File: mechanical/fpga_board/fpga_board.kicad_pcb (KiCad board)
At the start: 4 copper layers, 100 x 100 mm, 36 parts, among them J1 Conn_02x17_Odd_Even, J2 Conn_02x17_Odd_Even, J3 Conn_02x17_Odd_Even, J4 Conn_02x17_Odd_Even, J5 Conn_02x17_Odd_Even, J6 jtag, J7 Conn_02x03_Odd_Even, U1 XC6SLX16-FTG256

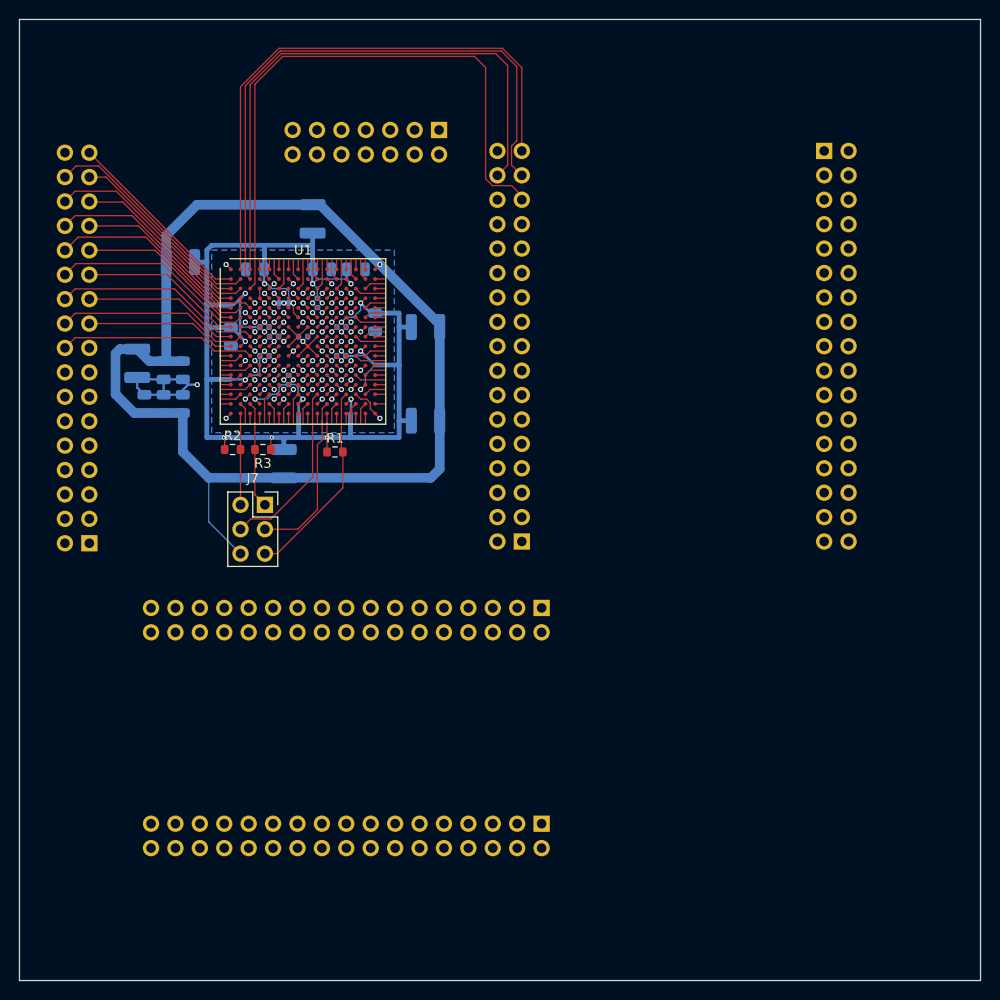
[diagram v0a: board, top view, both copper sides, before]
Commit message: all fpga pins routed, still need regulators
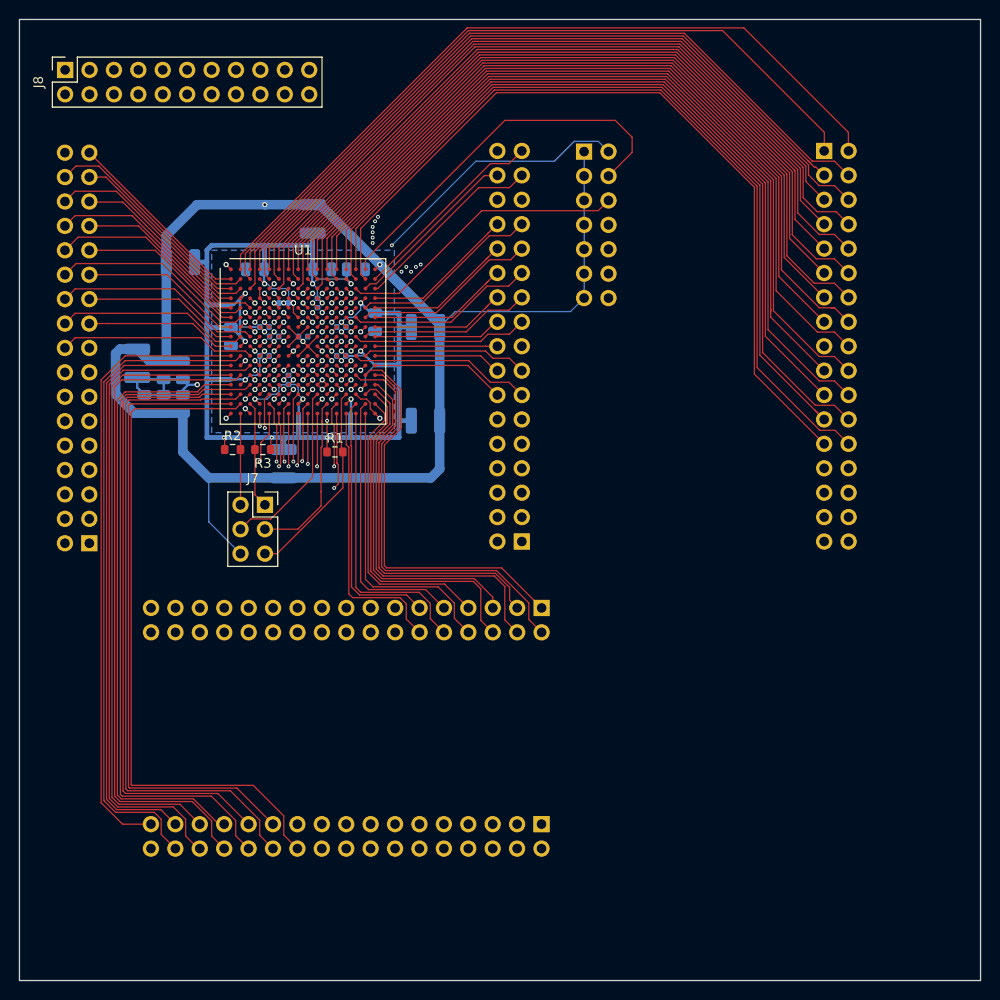
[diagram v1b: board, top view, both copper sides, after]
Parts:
- added J8: Conn_02x12_Odd_Even, Connector_PinSocket_2.54mm:PinSocket_2x11_P2.54mm_Vertical, F.Cu at (243.3, 160.0)
- moved J6 15.3 mm to (297.3, 168.5), turned to 180 degrees
- moved J4 0.05 mm to (292.9, 238.5)
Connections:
- U1 pad A10: Net-(U1-PadA10) -> /T16+3
- U1 pad A11: Net-(U1-PadA11) -> /T12+3
- U1 pad A12: Net-(U1-PadA12) -> /T11+3
- U1 pad A13: Net-(U1-PadA13) -> /T13+3
- U1 pad A14: Net-(U1-PadA14) -> /T16-3
- U1 pad A2: /T9-1 -> /T5+3
- U1 pad A3: /T13-1 -> /T6+3
- U1 pad A4: /T14-1 -> /T7+3
- U1 pad A5: Net-(U1-PadA5) -> /T8+3
- U1 pad A6: Net-(U1-PadA6) -> /T5-3
- U1 pad A7: Net-(U1-PadA7) -> /T6-3
- U1 pad A8: Net-(U1-PadA8) -> /T7-3
- U1 pad A9: Net-(U1-PadA9) -> /T8-3
- U1 pad B10: Net-(U1-PadB10) -> /T4-3
- U1 pad B12: Net-(U1-PadB12) -> /T14+3
- U1 pad B14: Net-(U1-PadB14) -> /T10+3
- U1 pad B15: Net-(U1-PadB15) -> /T9+3
- U1 pad B16: Net-(U1-PadB16) -> /T9-1
- U1 pad B3: /T10-1 -> /T1+3
- U1 pad B5: Net-(U1-PadB5) -> /T3+3
- U1 pad B6: Net-(U1-PadB6) -> /T4+3
- U1 pad B8: Net-(U1-PadB8) -> /T2-3
- U1 pad C10: Net-(U1-PadC10) -> /T15+3
- U1 pad C11: Net-(U1-PadC11) -> /T11-3
- U1 pad C13: Net-(U1-PadC13) -> /extra19
- U1 pad C15: Net-(U1-PadC15) -> /T13-1
- U1 pad C16: Net-(U1-PadC16) -> /T10-1
- U1 pad C3: /T11-1 -> /T2+3
- U1 pad C5: Net-(U1-PadC5) -> /extra5
- U1 pad C6: Net-(U1-PadC6) -> /T1-3
- U1 pad C7: Net-(U1-PadC7) -> /extra9
- U1 pad C8: Net-(U1-PadC8) -> /T3-3
- U1 pad C9: Net-(U1-PadC9) -> /T15-3
- U1 pad D11: Net-(U1-PadD11) -> /T10-3
- U1 pad D12: Net-(U1-PadD12) -> /T9-3
- U1 pad D14: Net-(U1-PadD14) -> /T14-1
- U1 pad D16: Net-(U1-PadD16) -> /T15-1
- U1 pad D5: Net-(U1-PadD5) -> /extra1
- U1 pad D6: Net-(U1-PadD6) -> /extra7
- U1 pad D8: Net-(U1-PadD8) -> /extra11
- U1 pad D9: Net-(U1-PadD9) -> /T12-3
- U1 pad E10: Net-(U1-PadE10) -> /T14-3
- U1 pad E11: Net-(U1-PadE11) -> /T13-3
- U1 pad E12: Net-(U1-PadE12) -> /T11-1
- U1 pad E13: Net-(U1-PadE13) -> /T2-1
- U1 pad E15: Net-(U1-PadE15) -> /T12-1
- U1 pad E16: Net-(U1-PadE16) -> /T16-1
- U1 pad E6: Net-(U1-PadE6) -> /extra3
- U1 pad E7: Net-(U1-PadE7) -> /extra4
- U1 pad E8: Net-(U1-PadE8) -> /extra8
- U1 pad F10: Net-(U1-PadF10) -> /extra10
- U1 pad F12: Net-(U1-PadF12) -> /extra14
- U1 pad F13: Net-(U1-PadF13) -> /T6-1
- U1 pad F14: Net-(U1-PadF14) -> /T10+1
- U1 pad F15: Net-(U1-PadF15) -> /T9+1
- U1 pad F16: Net-(U1-PadF16) -> /T13+1
- U1 pad F7: Net-(U1-PadF7) -> /extra2
- U1 pad F9: Net-(U1-PadF9) -> /extra12
- U1 pad G11: Net-(U1-PadG11) -> /extra6
- U1 pad G12: Net-(U1-PadG12) -> /extra16
- U1 pad G14: Net-(U1-PadG14) -> /T1-1
- U1 pad G16: Net-(U1-PadG16) -> /T14+1
- U1 pad H11: Net-(U1-PadH11) -> /extra13
- U1 pad H13: Net-(U1-PadH13) -> /extra15
- U1 pad H14: Net-(U1-PadH14) -> /T12+1
- U1 pad H15: Net-(U1-PadH15) -> /T11+1
- U1 pad H16: Net-(U1-PadH16) -> /T15+1
- U1 pad J11: Net-(U1-PadJ11) -> /extra17
- U1 pad J12: Net-(U1-PadJ12) -> /T5-1
- U1 pad J13: Net-(U1-PadJ13) -> /T4+1
- U1 pad J14: Net-(U1-PadJ14) -> /T8+1
- U1 pad J16: Net-(U1-PadJ16) -> /T16+1
- U1 pad K1: Net-(U1-PadK1) -> /T9-4
- U1 pad K11: Net-(U1-PadK11) -> /extra18
- U1 pad K12: Net-(U1-PadK12) -> /T3+1
- U1 pad K14: Net-(U1-PadK14) -> /T3-1
- U1 pad K15: Net-(U1-PadK15) -> /T4-1
- U1 pad K16: Net-(U1-PadK16) -> /T8-1
- U1 pad K2: Net-(U1-PadK2) -> /T13-4
- U1 pad K5: Net-(U1-PadK5) -> /T11+4
- U1 pad L1: Net-(U1-PadL1) -> /T10-4
- U1 pad L10: Net-(U1-PadL10) -> /T2+4
- U1 pad L12: Net-(U1-PadL12) -> /T6+1
- U1 pad L13: Net-(U1-PadL13) -> /T7+1
- U1 pad L14: Net-(U1-PadL14) -> /T2+1
- U1 pad L16: Net-(U1-PadL16) -> /T7-1
- U1 pad L3: Net-(U1-PadL3) -> /T14-4
- U1 pad L5: Net-(U1-PadL5) -> /T12+4
- U1 pad L7: Net-(U1-PadL7) -> /T4+4
- U1 pad L8: Net-(U1-PadL8) -> /T3+4
- U1 pad M1: Net-(U1-PadM1) -> /T11-4
- U1 pad M10: Net-(U1-PadM10) -> /T6+4
- U1 pad M11: Net-(U1-PadM11) -> /T1+4
- U1 pad M12: Net-(U1-PadM12) -> /T5+4
- U1 pad M13: Net-(U1-PadM13) -> /T1+1
- U1 pad M14: Net-(U1-PadM14) -> /T2+5
- U1 pad M15: Net-(U1-PadM15) -> /T1+5
- U1 pad M16: Net-(U1-PadM16) -> /T5+5
- U1 pad M2: Net-(U1-PadM2) -> /T15-4
- U1 pad M3: Net-(U1-PadM3) -> /T16+4
- U1 pad M4: Net-(U1-PadM4) -> /T15+4
- U1 pad M5: Net-(U1-PadM5) -> /T4-4
- U1 pad M6: Net-(U1-PadM6) -> /T6-4
- U1 pad M7: Net-(U1-PadM7) -> /T7+4
- U1 pad M9: Net-(U1-PadM9) -> /T15+5
- U1 pad N1: Net-(U1-PadN1) -> /T12-4
- U1 pad N12: Net-(U1-PadN12) -> /T3-5
- U1 pad N14: Net-(U1-PadN14) -> /T5+1
- U1 pad N16: Net-(U1-PadN16) -> /T6+5
- U1 pad N3: Net-(U1-PadN3) -> /T16-4
- U1 pad N4: Net-(U1-PadN4) -> /T8-4
- U1 pad N5: Net-(U1-PadN5) -> /T5-4
- U1 pad N6: Net-(U1-PadN6) -> /T14+5
- U1 pad N8: Net-(U1-PadN8) -> /T12+5
- U1 pad N9: Net-(U1-PadN9) -> /T8-5
- U1 pad P1: Net-(U1-PadP1) -> /T9+4
- U1 pad P11: Net-(U1-PadP11) -> /T7-5
- U1 pad P12: Net-(U1-PadP12) -> /T4-5
- U1 pad P15: Net-(U1-PadP15) -> /T3+5
- U1 pad P16: Net-(U1-PadP16) -> /T7+5
- U1 pad P2: Net-(U1-PadP2) -> /T13+4
- U1 pad P4: Net-(U1-PadP4) -> /T7-4
- U1 pad P5: Net-(U1-PadP5) -> /T8+4
- U1 pad P6: Net-(U1-PadP6) -> /T2-4
- U1 pad P7: Net-(U1-PadP7) -> /T11+5
- U1 pad P8: Net-(U1-PadP8) -> /T15-5
- U1 pad P9: Net-(U1-PadP9) -> /T16+5
- U1 pad R1: Net-(U1-PadR1) -> /T10+4
- U1 pad R12: Net-(U1-PadR12) -> /T10+5
- U1 pad R14: Net-(U1-PadR14) -> /T2-5
- U1 pad R15: Net-(U1-PadR15) -> /T1-5
- U1 pad R16: Net-(U1-PadR16) -> /T4+5
- U1 pad R2: Net-(U1-PadR2) -> /T14+4
- U1 pad R5: Net-(U1-PadR5) -> /T13-5
- U1 pad R7: Net-(U1-PadR7) -> /T14-5
- U1 pad R9: Net-(U1-PadR9) -> /T16-5
- U1 pad T10: Net-(U1-PadT10) -> /T13+5
- U1 pad T12: Net-(U1-PadT12) -> /extra20
- U1 pad T13: Net-(U1-PadT13) -> /T6-5
- U1 pad T14: Net-(U1-PadT14) -> /T5-5
- U1 pad T15: Net-(U1-PadT15) -> /T8+5
- U1 pad T3: Net-(U1-PadT3) -> /T3-4
- U1 pad T4: Net-(U1-PadT4) -> /T1-4
- U1 pad T5: Net-(U1-PadT5) -> /T9-5
- U1 pad T6: Net-(U1-PadT6) -> /T10-5
- U1 pad T7: Net-(U1-PadT7) -> /T11-5
- U1 pad T8: Net-(U1-PadT8) -> /T12-5
- U1 pad T9: Net-(U1-PadT9) -> /T9+5
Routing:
- net /T5+4: track 0.00 -> 110.5 mm, vias 0 -> 1
- net /T1+4: track 0.00 -> 109.6 mm, vias 0 -> 1
- net /T13-3: track 0.00 -> 109.6 mm, vias 0 -> 1
- net /T9-3: track 0.00 -> 108.2 mm, vias 0 -> 1
- net /T14-3: track 0.00 -> 107.6 mm, vias 0 -> 1
- net /T15-3: track 0.00 -> 105.9 mm, vias 0 -> 1
- net /T6+4: track 0.00 -> 105.6 mm, vias 0 -> 1
- net /T2+4: track 0.00 -> 105.2 mm, vias 0 -> 1
- net /T10-3: track 0.00 -> 104.2 mm, vias 0 -> 1
- net /T11-3: track 0.00 -> 103.5 mm, vias 0 -> 1
- net /T12-3: track 0.00 -> 103.2 mm, vias 0 -> 1
- net /T7+4: track 0.00 -> 101.5 mm, vias 0 -> 1
- net /T3+4: track 0.00 -> 100.5 mm, vias 0 -> 1
- net /T4+4: track 0.00 -> 96.5 mm, vias 0 -> 1
- net /T8+4: track 0.00 -> 91.6 mm, vias 0 -> 1
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
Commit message: Moved FPGA and added hole
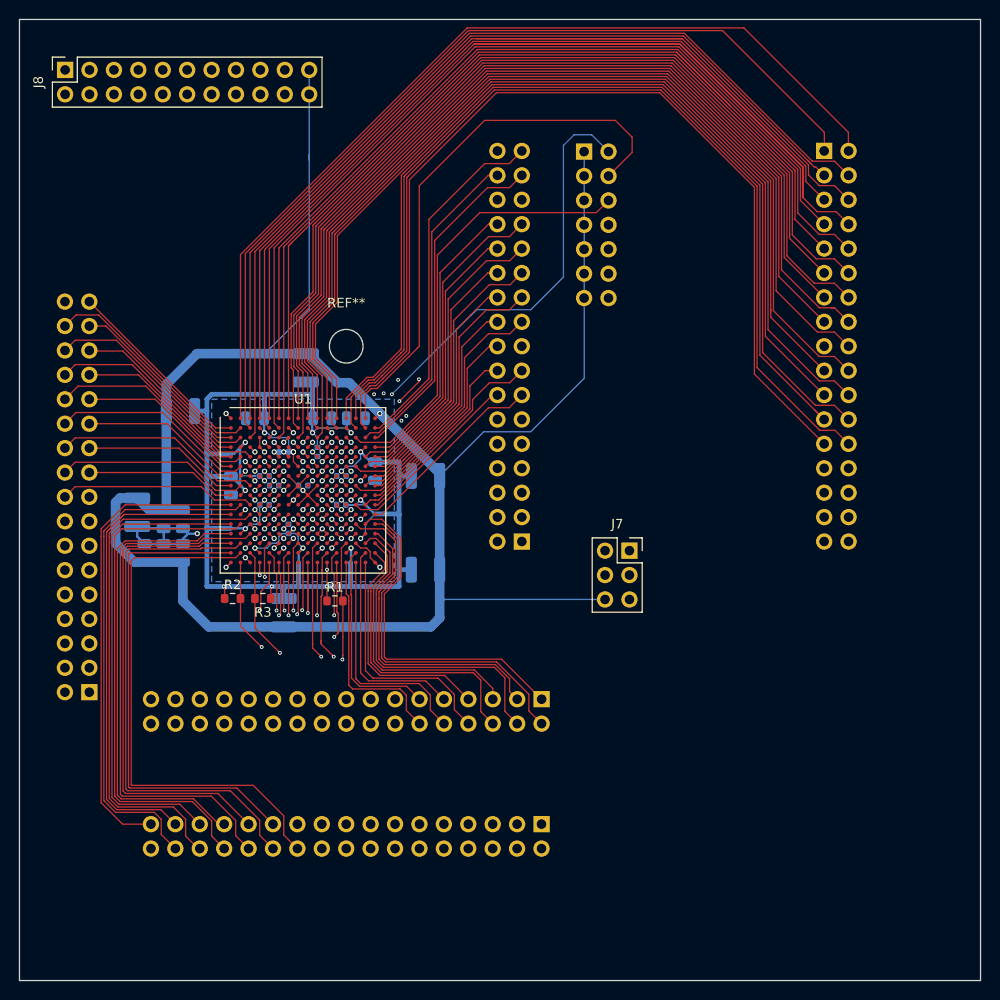
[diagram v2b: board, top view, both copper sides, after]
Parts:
- added REF**: MountingHole_3.5mm, MountingHole:MountingHole_3.5mm, F.Cu at (272.5, 188.7)
- moved J7 38.2 mm to (302.0, 210.0)
- moved C11 15.5 mm to (268.3, 191.0)
- moved C1 15.5 mm to (280.8, 212.0)
- moved C10 15.5 mm to (266.5, 207.7)
- moved C12 15.5 mm to (270.0, 196.2)
- moved C13 15.5 mm to (264.0, 205.2)
- moved C14 15.5 mm to (264.0, 202.2)
- moved C15 15.5 mm to (280.8, 202.2)
- moved C16 15.5 mm to (260.5, 203.2)
- moved C17 15.5 mm to (266.0, 199.7)
- moved C18 15.5 mm to (265.0, 203.2)
- moved C19 15.5 mm to (268.1, 203.2)
- moved C2 15.5 mm to (273.5, 196.2)
- moved C20 15.5 mm to (255.5, 206.7)
- moved C21 15.5 mm to (253.5, 210.2)
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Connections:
- U1 pad E13: /T2-1 -> /T6-1
- U1 pad F13: /T6-1 -> /T2-1
- U1 pad G14: /T1-1 -> /T5-1
- U1 pad J11: /extra17 -> /glckorsomething
- U1 pad J12: /T5-1 -> /T1-1
- U1 pad J13: /T4+1 -> /T8+1
- U1 pad J14: /T8+1 -> /T4+1
- U1 pad K12: /T3+1 -> /T7+1
- U1 pad K14: /T3-1 -> /T7-1
- U1 pad K15: /T4-1 -> /T8-1
- U1 pad K16: /T8-1 -> /T4-1
- U1 pad L12: /T6+1 -> /T2+1
- U1 pad L13: /T7+1 -> /T3+1
- U1 pad L14: /T2+1 -> /T6+1
- U1 pad L16: /T7-1 -> /T3-1
- U1 pad M13: /T1+1 -> /T5+1
- U1 pad N14: /T5+1 -> /T1+1
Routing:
- net /T8+3: track 80.8 -> 139.1 mm
- net /init_b: track 11.1 -> 53.1 mm, vias 0 -> 1
- net /program_b: track 9.50 -> 49.6 mm, vias 0 -> 1
- net /T7+3: track 79.9 -> 119.0 mm
- net /gnd: track 195.2 -> 231.3 mm, vias 26 -> 25
- net /cclk: track 18.0 -> 47.7 mm, vias 0 -> 1
- net /din: track 18.6 -> 47.3 mm, vias 0 -> 1
- net /extra6: track 37.7 -> 61.8 mm
- net /done: track 21.0 -> 45.0 mm, vias 0 -> 1
- net /T1-3: track 80.7 -> 104.2 mm
- net /extra19: track 42.3 -> 63.7 mm
- net /extra10: track 30.9 -> 50.0 mm
- net /extra20: track 71.7 -> 89.7 mm, vias 3 -> 1
- net /extra12: track 31.6 -> 49.6 mm
- net /extra8: track 31.8 -> 49.7 mm
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
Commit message: Added mounting holes, reduced size on FPGA board
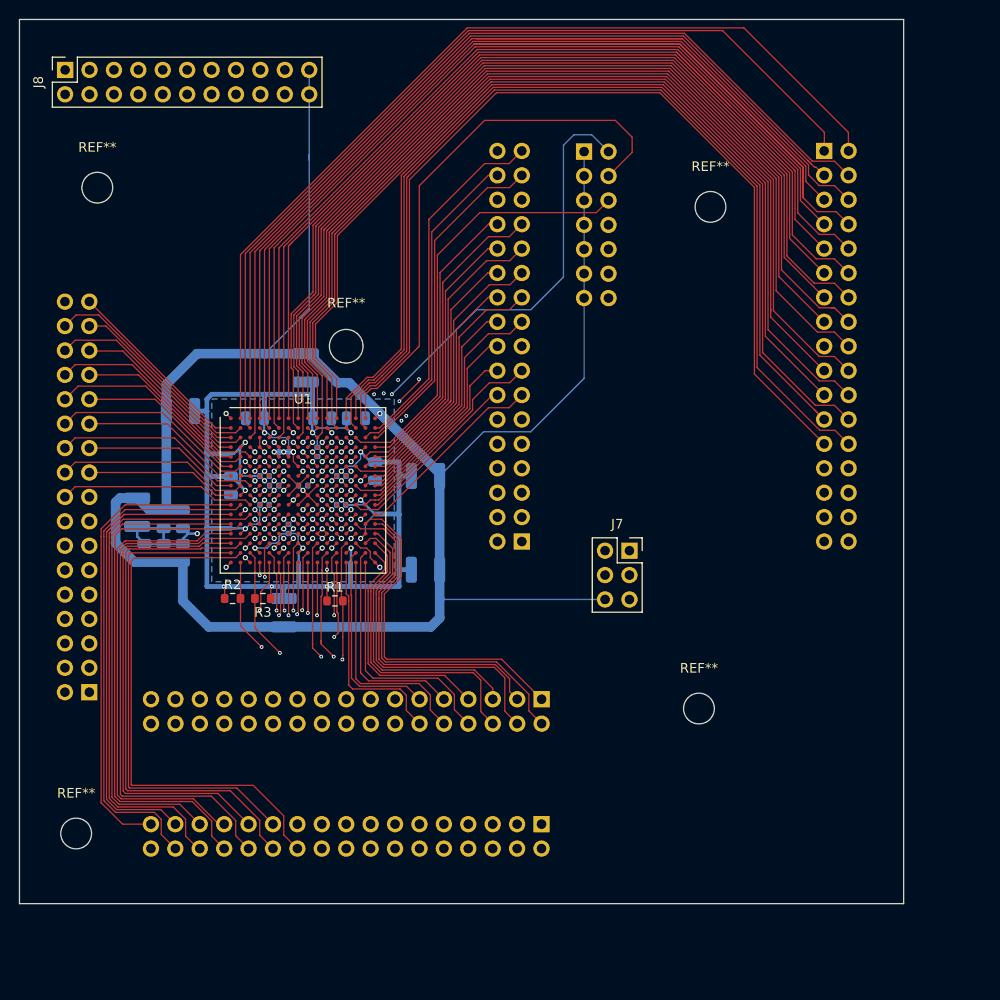
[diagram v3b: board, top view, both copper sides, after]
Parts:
- added REF**: MountingHole_3.2mm_M3, MountingHole:MountingHole_3.2mm_M3, F.Cu at (244.4, 239.4)
- added REF**: MountingHole_3.2mm_M3, MountingHole:MountingHole_3.2mm_M3, F.Cu at (309.2, 226.4)
- added REF**: MountingHole_3.2mm_M3, MountingHole:MountingHole_3.2mm_M3, F.Cu at (310.4, 174.2)
- added REF**: MountingHole_3.2mm_M3, MountingHole:MountingHole_3.2mm_M3, F.Cu at (246.6, 172.2)
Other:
- board size 100 x 100 mm -> 92 x 92 mm

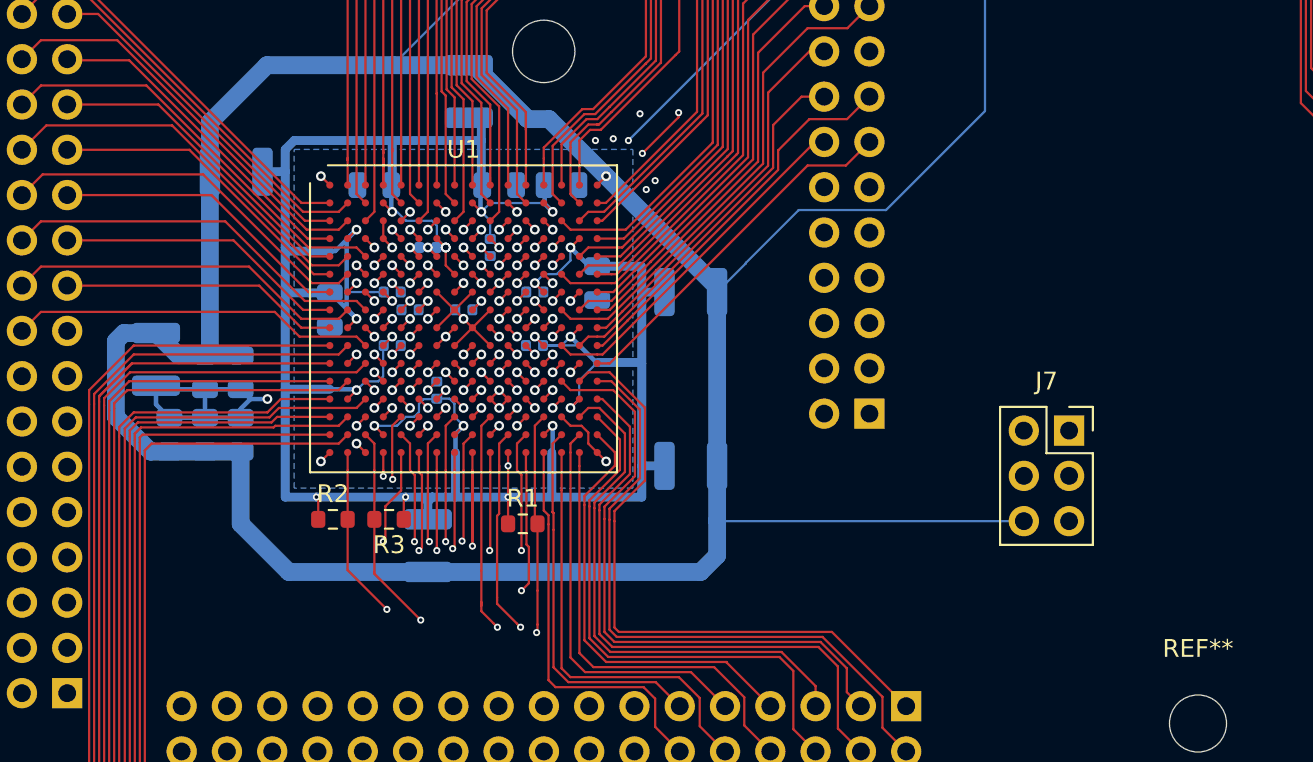
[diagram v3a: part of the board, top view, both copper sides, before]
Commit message: Added linear regulators and oscillator
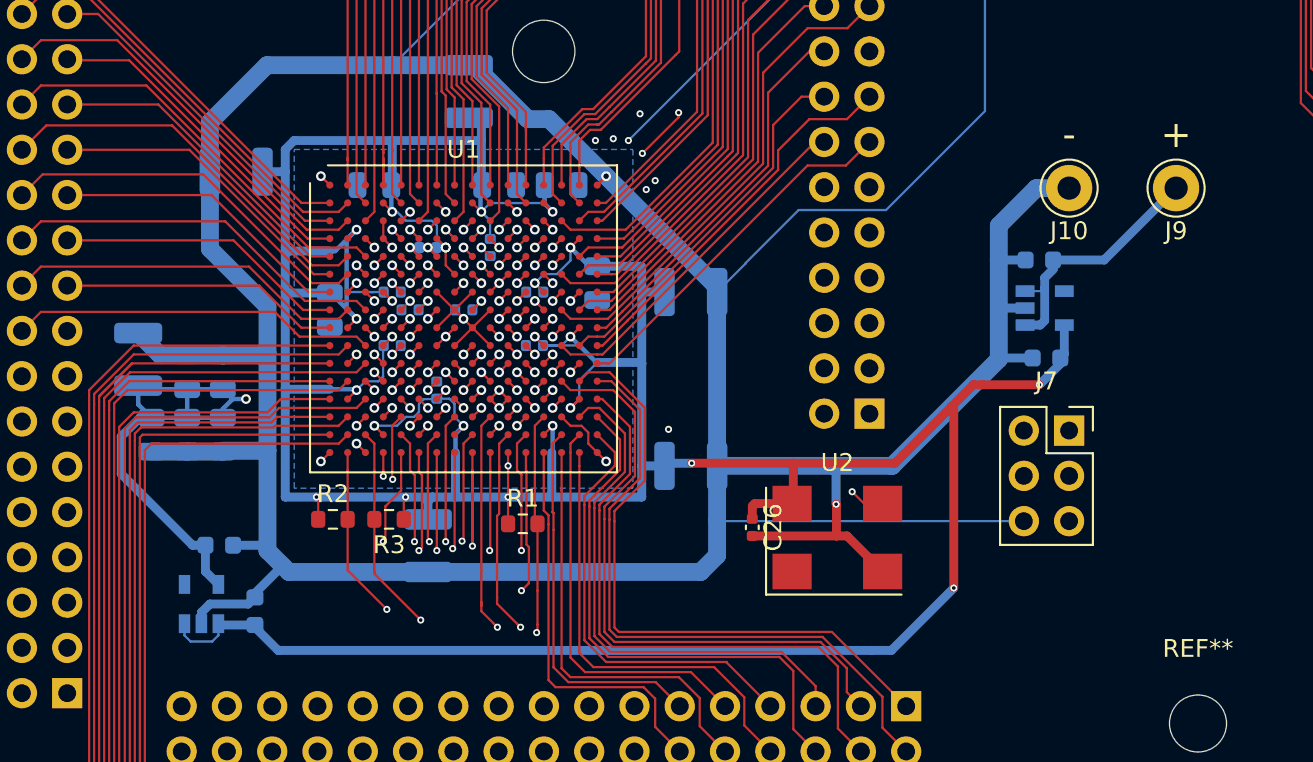
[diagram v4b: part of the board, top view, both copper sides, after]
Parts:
- added C26: 0u1, Capacitor_SMD:C_0402_1005Metric, F.Cu at (284.2, 215.4)
- added C27: 1u, Capacitor_SMD:C_0603_1608Metric, B.Cu at (300.3, 200.4)
- added C28: 1u, Capacitor_SMD:C_0603_1608Metric, B.Cu at (256.3, 220.1)
- added C29: 1u, Capacitor_SMD:C_0603_1608Metric, B.Cu at (300.7, 205.9)
- added C30: 1u, Capacitor_SMD:C_0603_1608Metric, B.Cu at (254.3, 216.4)
- added J10: Conn_01x01, Connector_Pin:Pin_D1.3mm_L11.0mm, F.Cu at (302.0, 196.4)
- added J9: Conn_01x01, Connector_Pin:Pin_D1.3mm_L11.0mm, F.Cu at (308.0, 196.4)
- added U2: SiT1602, FPGA_Board_Footprints:SiT1602_7_5, F.Cu at (289.0, 216.0)
- added U3: MIC5504-3.3YM5, Package_TO_SOT_SMD:SOT-23-5, B.Cu at (300.6, 203.1)
- added U4: MIC5504-1.2YM5, Package_TO_SOT_SMD:SOT-23-5, B.Cu at (253.3, 219.7)
- moved C20 1.00 mm to (254.5, 206.7)
- moved C21 1.00 mm to (252.5, 210.2)
- moved C22 1.00 mm to (254.5, 210.2)
- moved C23 1.00 mm to (250.5, 210.2)
- moved C24 1.00 mm to (252.5, 206.7)
- moved C25 1.00 mm to (249.8, 206.0)
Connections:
- U1 pad J11: /glckorsomething -> /extra17
- U1 pad K11: /extra18 -> /clk
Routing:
- net /vcc: track 280.1 -> 369.7 mm, vias 33 -> 36
- net /extra18: track 67.9 -> 0.00 mm, vias 1 -> 0
- net /gnd: track 231.3 -> 288.0 mm, vias 25 -> 26
- net /clk: track 0.00 -> 24.7 mm, vias 0 -> 3
- net /vin: track 0.00 -> 14.6 mm
- net /vcc2: track 46.8 -> 60.9 mm
- net /T1+1: track 26.8 -> 19.8 mm
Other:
- board text added: "+"
- board text added: "-"
